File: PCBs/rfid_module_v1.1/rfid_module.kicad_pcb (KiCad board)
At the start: 4 copper layers, 22.3 x 13.9 mm, 66 parts, among them IC201 TLV9004SIRTER, IC202 MAX9027EBT+T, IC501 MAX17291BANT+T, J401 10-Pin_Pogo_Connector_Male, Q201 DMN21D2UFB-7B, Q202 DMP21D5UFB4-7B, Q203 DMN21D2UFB-7B, Q204 DMN21D2UFB-7B, Q401 DMN21D2UFB-7B, U101 Watch_Module_Outline_V2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

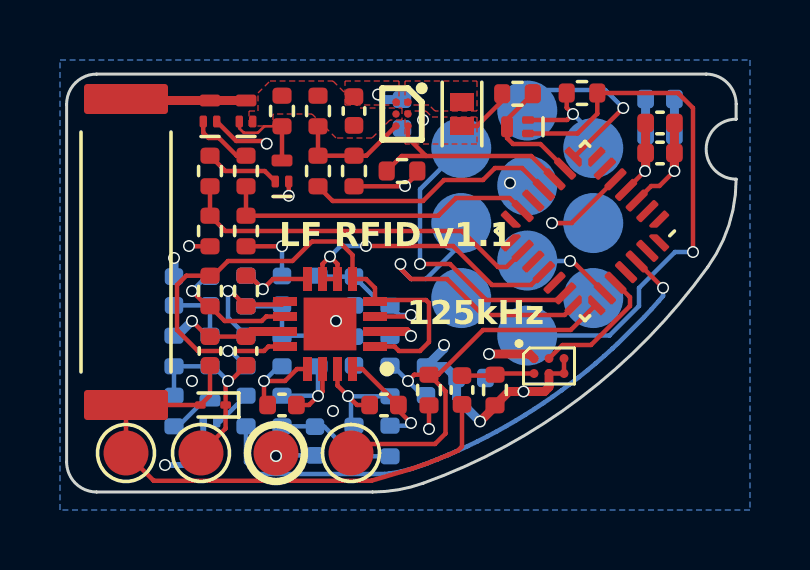
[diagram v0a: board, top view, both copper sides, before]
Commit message: RFID Module v1.1 complete (+default firmware)
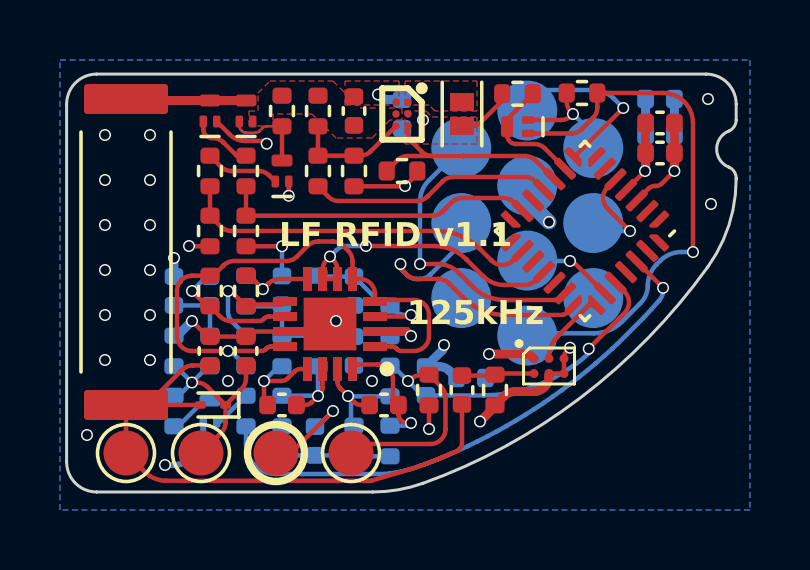
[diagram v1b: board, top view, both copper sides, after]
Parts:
- turned C210 to 90 degrees
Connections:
- U301 pad 22: /RFID/RF_IN -> /RFID/CARRIER
- U301 pad 24: /RFID/CARRIER -> /RFID/RF_IN
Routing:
- net GND: track 32.6 -> 36.0 mm, vias 18 -> 33
- net /RFID/RF_IN: track 14.5 -> 16.7 mm, vias 1 -> 2
- net /RFID/CARRIER: track 4.40 -> 2.50 mm
- net /RFID/RF: track 18.7 -> 20.5 mm
- net /Boost Converter/EN: track 7.37 -> 8.52 mm
- net /RFID/SIGNAL_ENVELOPE: track 6.57 -> 7.55 mm
- net /RFID/AMP3_NEG: track 3.54 -> 4.22 mm
- net /Pogo Connector/NRST: track 4.10 -> 3.54 mm
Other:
- outline, holes or cut-outs redrawn
